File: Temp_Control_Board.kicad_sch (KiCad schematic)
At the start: 34 parts, among them J1 OVEN_INTERFACE, J2 OLED, J3 USB_B_Micro, J4 MICROSD, SW1 BOOT, SW2 EN, U1 ESP-WROOM-32, U2 AZ1117EH-3.3TRG1, U3 ROTARY_ENC_PEC12R, U4 FT232RLREEL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

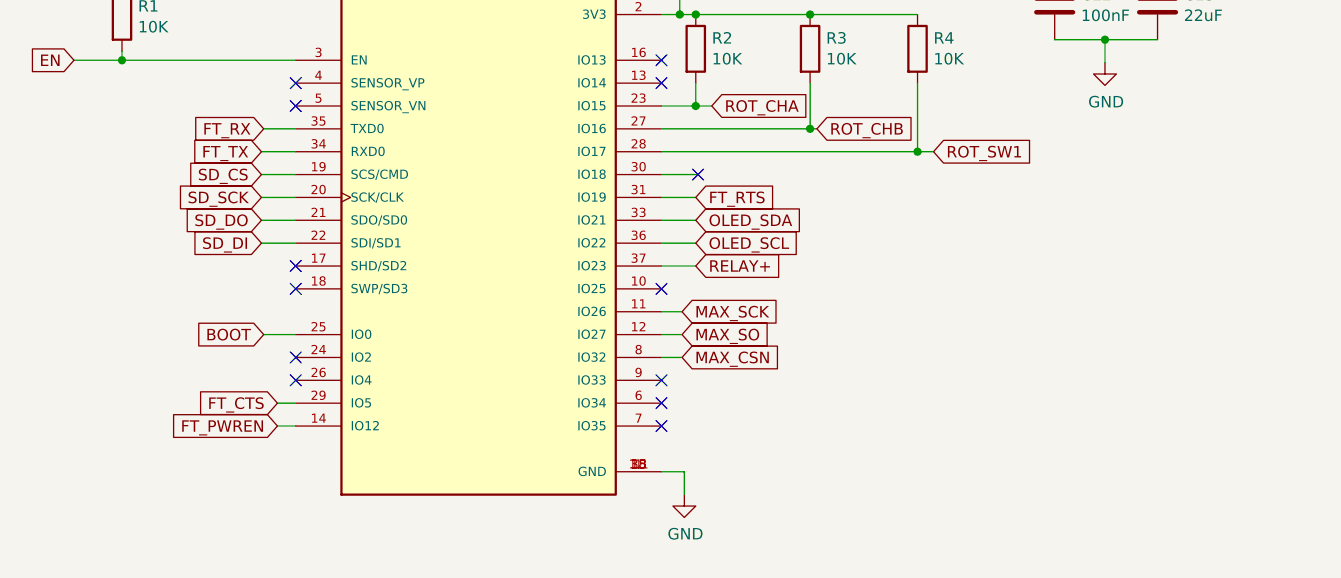
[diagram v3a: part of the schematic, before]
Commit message: sch: changed SD card pis to use SPI3 (VSPI)
    - Moved FT232 RTS and CTS pins to floating for now. These
      should be tied into the reset-esp32-via-UART circuit
      anyway
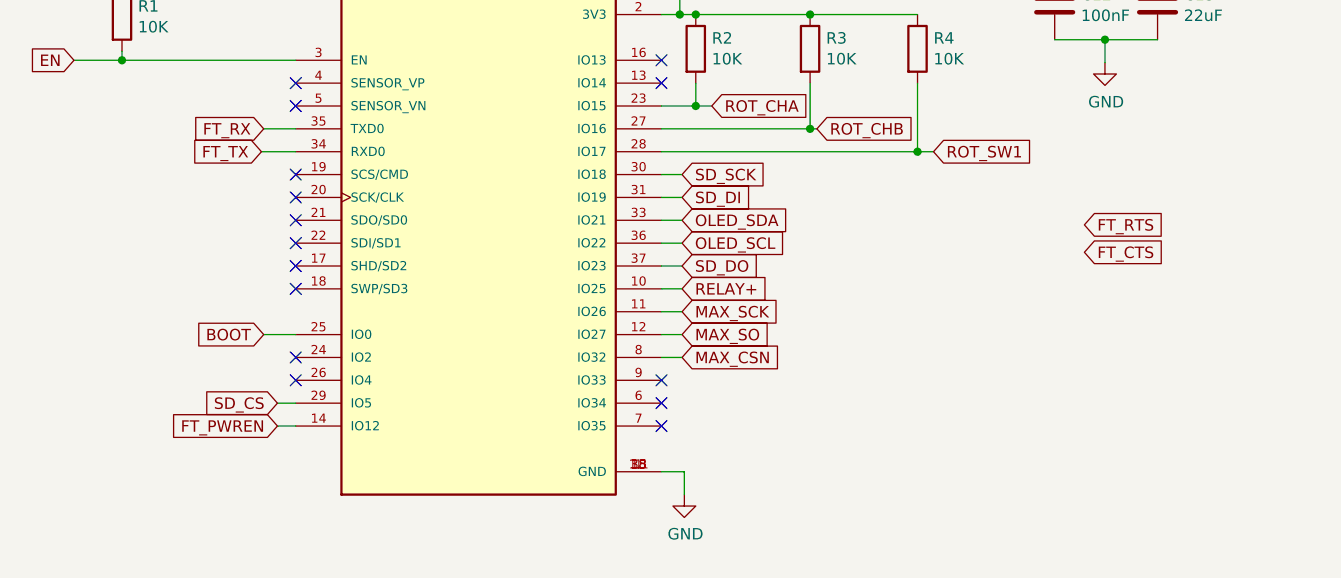
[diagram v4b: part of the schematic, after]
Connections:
- net FT_CTS: no longer U1.29 (IO5)
- net FT_RTS: no longer U1.31 (IO19)
- net RELAY+: now also U1.10 (IO25); no longer U1.37 (IO23)
- net SD_CS: now also U1.29 (IO5); no longer U1.19 (SCS/CMD)
- net SD_DI: now also U1.31 (IO19); no longer U1.22 (SDI/SD1)
- net SD_DO: now also U1.37 (IO23); no longer U1.21 (SDO/SD0)
- net SD_SCK: now also U1.30 (IO18); no longer U1.20 (SCK/CLK)
- no-connect marks 26 -> 28
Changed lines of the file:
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@@
   (junction (at 153.416 44.196) (diameter 0) (color 0 0 0 0)
   )
+  (no_connect (at 63.5 61.722))
+  (no_connect (at 63.5 66.802))
+  (no_connect (at 104.14 87.122))
   (no_connect (at 330.708 53.086))
+  (no_connect (at 63.5 64.262))
   (no_connect (at 284.988 60.706))
   (no_connect (at 104.14 46.482))
@@
   (no_connect (at 104.14 82.042))
   (no_connect (at 73.406 224.536))
+  (no_connect (at 63.5 69.342))
+  (no_connect (at 63.5 71.882))
   (no_connect (at 63.5 82.042))
   (no_connect (at 63.5 51.562))
-  (no_connect (at 104.14 87.122))
   (no_connect (at 104.14 49.022))
   (no_connect (at 330.708 48.006))
   (no_connect (at 284.988 73.406))
-  (no_connect (at 63.5 71.882))
   (no_connect (at 284.988 63.246))
   (no_connect (at 330.708 73.406))
-  (no_connect (at 63.5 69.342))
   (no_connect (at 284.988 53.086))
+  (no_connect (at 63.5 59.182))
   (no_connect (at 104.14 84.582))
-  (no_connect (at 108.204 59.182))
   (no_connect (at 63.5 49.022))
   (no_connect (at 330.708 63.246))
-  (no_connect (at 104.14 71.882))
   (no_connect (at 63.5 79.502))
   (polyline (pts (xy 223.774 117.094) (xy 302.26 117.094))
@@
     (stroke (width 0) (type default) (color 0 0 0 0))
   )
-  (wire (pts (xy 59.69 61.722) (xy 63.5 61.722))
-    (stroke (width 0) (type default) (color 0 0 0 0))
-  )
   (wire (pts (xy 251.714 82.55) (xy 245.618 82.55))
     (stroke (width 0) (type default) (color 0 0 0 0))
@@
     (stroke (width 0) (type default) (color 0 0 0 0))
   )
-  (wire (pts (xy 104.14 69.342) (xy 107.95 69.342))
-    (stroke (width 0) (type default) (color 0 0 0 0))
-  )
   (wire (pts (xy 153.416 44.196) (xy 153.416 46.736))
     (stroke (width 0) (type default) (color 0 0 0 0))
@@
     (stroke (width 0) (type default) (color 0 0 0 0))
   )
+  (wire (pts (xy 104.14 66.802) (xy 106.426 66.802))
+    (stroke (width 0) (type default) (color 0 0 0 0))
+  )
   (polyline (pts (xy 162.56 142.748) (xy 208.28 142.748))
     (stroke (width 0) (type default) (color 0 0 0 0))
@@
     (stroke (width 0) (type default) (color 0 0 0 0))
   )
+  (wire (pts (xy 104.14 61.722) (xy 106.426 61.722))
+    (stroke (width 0) (type default) (color 0 0 0 0))
+  )
   (polyline (pts (xy 302.26 117.094) (xy 302.26 153.924))
     (stroke (width 0) (type default) (color 0 0 0 0))
@@
     (stroke (width 0) (type default) (color 0 0 0 0))
   )
-  (wire (pts (xy 59.69 64.262) (xy 63.5 64.262))
-    (stroke (width 0) (type default) (color 0 0 0 0))
-  )
   (wire (pts (xy 147.828 44.196) (xy 153.416 44.196))
     (stroke (width 0) (type default) (color 0 0 0 0))
@@
     (stroke (width 0) (type default) (color 0 0 0 0))
   )
+  (wire (pts (xy 104.14 71.882) (xy 106.426 71.882))
+    (stroke (width 0) (type default) (color 0 0 0 0))
+  )
   (wire (pts (xy 138.43 141.732) (xy 147.574 141.732))
     (stroke (width 0) (type default) (color 0 0 0 0))
@@
     (stroke (width 0) (type default) (color 0 0 0 0))
   )
-  (wire (pts (xy 59.69 59.182) (xy 63.5 59.182))
-    (stroke (width 0) (type default) (color 0 0 0 0))
-  )
-  (wire (pts (xy 59.69 66.802) (xy 63.5 66.802))
-    (stroke (width 0) (type default) (color 0 0 0 0))
-  )
   (wire (pts (xy 284.988 68.326) (xy 284.988 70.866))
     (stroke (width 0) (type default) (color 0 0 0 0))
@@
     (stroke (width 0) (type default) (color 0 0 0 0))
   )
-  (wire (pts (xy 108.204 59.182) (xy 104.14 59.182))
-    (stroke (width 0) (type default) (color 0 0 0 0))
-  )
   (polyline (pts (xy 208.28 123.19) (xy 162.56 123.19))
     (stroke (width 0) (type default) (color 0 0 0 0))
@@
     (stroke (width 0) (type default) (color 0 0 0 0))
   )
-  (wire (pts (xy 104.14 61.722) (xy 107.95 61.722))
-    (stroke (width 0) (type default) (color 0 0 0 0))
-  )
   (wire (pts (xy 70.358 151.638) (xy 70.358 154.178))
     (stroke (width 0) (type default) (color 0 0 0 0))
@@
     (stroke (width 0) (type default) (color 0 0 0 0))
   )
+  (wire (pts (xy 104.14 69.342) (xy 106.426 69.342))
+    (stroke (width 0) (type default) (color 0 0 0 0))
+  )
   (wire (pts (xy 284.988 50.546) (xy 280.162 50.546))
     (stroke (width 0) (type default) (color 0 0 0 0))
@@
     (stroke (width 0) (type default) (color 0 0 0 0))
   )
-  (wire (pts (xy 104.14 66.802) (xy 107.95 66.802))
-    (stroke (width 0) (type default) (color 0 0 0 0))
-  )
   (wire (pts (xy 272.288 48.006) (xy 284.988 48.006))
     (stroke (width 0) (type default) (color 0 0 0 0))
@@
     (stroke (width 0) (type default) (color 0 0 0 0))
   )
+  (wire (pts (xy 104.14 59.182) (xy 106.426 59.182))
+    (stroke (width 0) (type default) (color 0 0 0 0))
+  )
   (polyline (pts (xy 154.432 151.384) (xy 154.432 121.158))
     (stroke (width 0) (type default) (color 0 0 0 0))
@@
     (stroke (width 0) (type default) (color 0 0 0 0))
   )
-  (wire (pts (xy 107.95 64.262) (xy 104.14 64.262))
+  (wire (pts (xy 104.14 64.262) (xy 106.426 64.262))
     (stroke (width 0) (type default) (color 0 0 0 0))
   )
@@
     (effects (font (size 1.27 1.27)) (justify left bottom))
   )
-  (global_label "RELAY+" (shape input) (at 107.95 69.342 0) (fields_autoplaced)
-    (effects (font (size 1.27 1.27)) (justify left))
-    (property "Intersheet References" "${INTERSHEET_REFS}" (id 0) (at 0 0 0)
-      (effects (font (size 1.27 1.27)) hide)
-    )
-  )
-  (global_label "FT_CTS" (shape input) (at 61.468 84.582 180) (fields_autoplaced)
-    (effects (font (size 1.27 1.27)) (justify right))
-    (property "Intersheet References" "${INTERSHEET_REFS}" (id 0) (at 0 0 0)
+  (global_label "RELAY+" (shape input) (at 106.426 71.882 0) (fields_autoplaced)
+    (effects (font (size 1.27 1.27)) (justify left))
+    (property "Intersheet References" "${INTERSHEET_REFS}" (id 0) (at -1.524 2.54 0)
+      (effects (font (size 1.27 1.27)) hide)
+    )
+  )
+  (global_label "FT_CTS" (shape input) (at 151.13 67.818 0) (fields_autoplaced)
+    (effects (font (size 1.27 1.27)) (justify left))
+    (property "Intersheet References" "${INTERSHEET_REFS}" (id 0) (at 212.598 152.4 0)
       (effects (font (size 1.27 1.27)) hide)
     )
@@
     )
   )
-  (global_label "SD_CS" (shape input) (at 59.69 59.182 180) (fields_autoplaced)
-    (effects (font (size 1.27 1.27)) (justify right))
-    (property "Intersheet References" "${INTERSHEET_REFS}" (id 0) (at 0 0 0)
+  (global_label "SD_CS" (shape input) (at 61.468 84.582 180) (fields_autoplaced)
+    (effects (font (size 1.27 1.27)) (justify right))
+    (property "Intersheet References" "${INTERSHEET_REFS}" (id 0) (at 1.778 25.4 0)
       (effects (font (size 1.27 1.27)) hide)
     )
@@
     )
   )
-  (global_label "SD_SCK" (shape input) (at 59.69 61.722 180) (fields_autoplaced)
-    (effects (font (size 1.27 1.27)) (justify right))
-    (property "Intersheet References" "${INTERSHEET_REFS}" (id 0) (at 0 0 0)
-      (effects (font (size 1.27 1.27)) hide)
-    )
-  )
-  (global_label "OLED_SCL" (shape input) (at 107.95 66.802 0) (fields_autoplaced)
-    (effects (font (size 1.27 1.27)) (justify left))
-    (property "Intersheet References" "${INTERSHEET_REFS}" (id 0) (at 0 0 0)
+  (global_label "SD_SCK" (shape input) (at 106.426 59.182 0) (fields_autoplaced)
+    (effects (font (size 1.27 1.27)) (justify left))
+    (property "Intersheet References" "${INTERSHEET_REFS}" (id 0) (at 166.116 120.904 0)
+      (effects (font (size 1.27 1.27)) hide)
+    )
+  )
+  (global_label "OLED_SCL" (shape input) (at 106.426 66.802 0) (fields_autoplaced)
+    (effects (font (size 1.27 1.27)) (justify left))
+    (property "Intersheet References" "${INTERSHEET_REFS}" (id 0) (at -1.524 0 0)
       (effects (font (size 1.27 1.27)) hide)
     )
@@
     )
   )
-  (global_label "OLED_SDA" (shape input) (at 107.95 64.262 0) (fields_autoplaced)
-    (effects (font (size 1.27 1.27)) (justify left))
-    (property "Intersheet References" "${INTERSHEET_REFS}" (id 0) (at 0 0 0)
+  (global_label "OLED_SDA" (shape input) (at 106.426 64.262 0) (fields_autoplaced)
+    (effects (font (size 1.27 1.27)) (justify left))
+    (property "Intersheet References" "${INTERSHEET_REFS}" (id 0) (at -1.524 0 0)
       (effects (font (size 1.27 1.27)) hide)
     )
@@
     )
   )
-  (global_label "FT_RTS" (shape input) (at 107.95 61.722 0) (fields_autoplaced)
-    (effects (font (size 1.27 1.27)) (justify left))
-    (property "Intersheet References" "${INTERSHEET_REFS}" (id 0) (at 0 0 0)
+  (global_label "FT_RTS" (shape input) (at 151.13 64.77 0) (fields_autoplaced)
+    (effects (font (size 1.27 1.27)) (justify left))
+    (property "Intersheet References" "${INTERSHEET_REFS}" (id 0) (at 43.18 3.048 0)
       (effects (font (size 1.27 1.27)) hide)
     )
@@
     )
   )
-  (global_label "SD_DO" (shape input) (at 59.69 64.262 180) (fields_autoplaced)
-    (effects (font (size 1.27 1.27)) (justify right))
-    (property "Intersheet References" "${INTERSHEET_REFS}" (id 0) (at 0 0 0)
+  (global_label "SD_DO" (shape input) (at 106.426 69.342 0) (fields_autoplaced)
+    (effects (font (size 1.27 1.27)) (justify left))
+    (property "Intersheet References" "${INTERSHEET_REFS}" (id 0) (at 166.116 133.604 0)
       (effects (font (size 1.27 1.27)) hide)
     )
@@
     )
   )
-  (global_label "SD_DI" (shape input) (at 59.69 66.802 180) (fields_autoplaced)
-    (effects (font (size 1.27 1.27)) (justify right))
-    (property "Intersheet References" "${INTERSHEET_REFS}" (id 0) (at 0 0 0)
-      (effects (font (size 1.27 1.27)) hide)
-    )
+  (global_label "SD_DI" (shape input) (at 106.426 61.722 0) (fields_autoplaced)
+    (effects (font (size 1.27 1.27)) (justify left))
+    (property "Intersheet References" "${INTERSHEET_REFS}" (id 0) (at 166.116 128.524 0)
+      (effects (font (size 1.27 1.27)) hide)
+    )

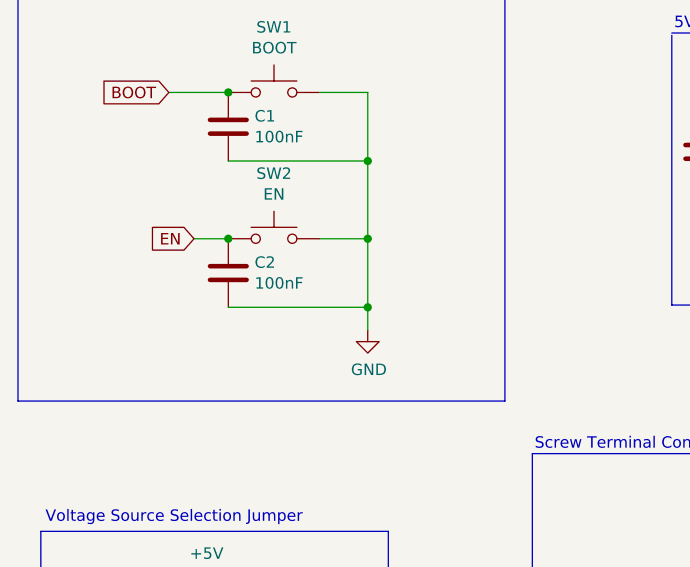
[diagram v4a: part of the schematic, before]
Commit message: sch: increased C between EN and GND
    - Necessary to increase capacitance for reset to work correctly
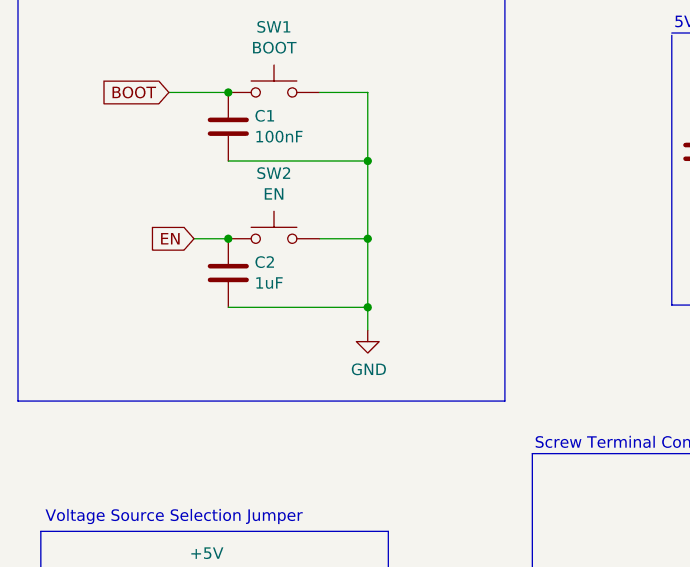
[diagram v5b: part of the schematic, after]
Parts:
- C2: value 100nF -> 1uF
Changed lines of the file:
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@@
       (effects (font (size 1.27 1.27)) (justify left))
     )
-    (property "Value" "100nF" (id 1) (at 57.785 148.971 0)
+    (property "Value" "1uF" (id 1) (at 57.785 148.971 0)
       (effects (font (size 1.27 1.27)) (justify left))
     )
@@
     )
     (path "/00000000-0000-0000-0000-0000607d89f7"
-      (reference "C2") (unit 1) (value "100nF") (footprint "Capacitor_SMD:C_0805_2012Metric_Pad1.15x1.40mm_HandSolder")
+      (reference "C2") (unit 1) (value "1uF") (footprint "Capacitor_SMD:C_0805_2012Metric_Pad1.15x1.40mm_HandSolder")
     )
     (path "/00000000-0000-0000-0000-0000607cc4d0"

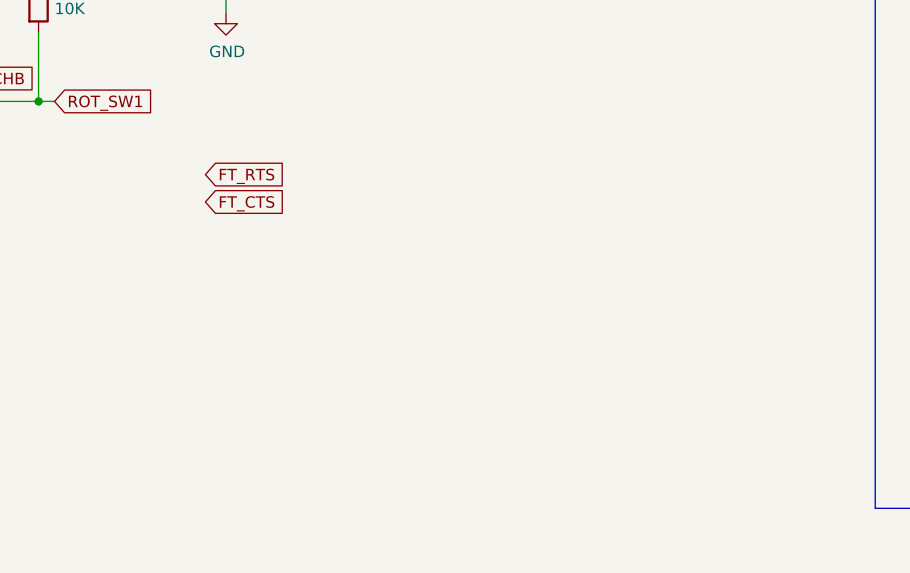
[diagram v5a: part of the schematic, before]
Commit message: Began adding reset circuit to schematic
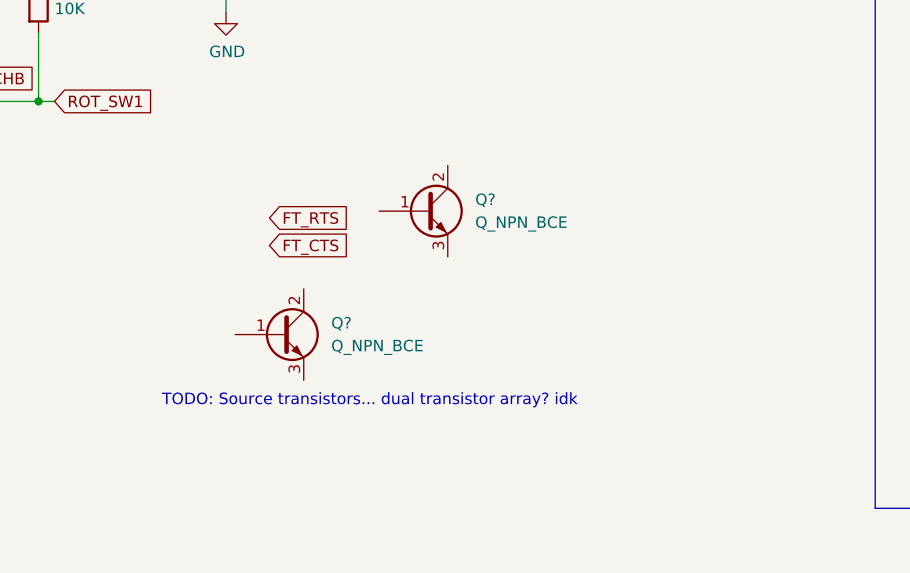
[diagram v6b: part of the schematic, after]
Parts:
- added Q? (x2): Q_NPN_BCE, symbol Device:Q_NPN_BCE
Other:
- note added: "TODO: Source transistors... dual transistor array? idk"
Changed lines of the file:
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@@
     (stroke (width 0) (type default) (color 0 0 0 0))
+  )
+  (text "TODO: Source transistors... dual transistor array? idk\n"
+    (at 146.304 90.678 0)
+    (effects (font (size 1.27 1.27)) (justify left bottom))
   )
   (text "Screw Terminal Connector" (at 88.9 167.64 0)
@@
     )
   )
-  (global_label "FT_CTS" (shape input) (at 151.13 67.818 0) (fields_autoplaced)
-    (effects (font (size 1.27 1.27)) (justify left))
-    (property "Intersheet References" "${INTERSHEET_REFS}" (id 0) (at 212.598 152.4 0)
+  (global_label "FT_CTS" (shape input) (at 158.242 72.644 0) (fields_autoplaced)
+    (effects (font (size 1.27 1.27)) (justify left))
+    (property "Intersheet References" "${INTERSHEET_REFS}" (id 0) (at 219.71 157.226 0)
       (effects (font (size 1.27 1.27)) hide)
     )
@@
     )
   )
-  (global_label "FT_RTS" (shape input) (at 151.13 64.77 0) (fields_autoplaced)
-    (effects (font (size 1.27 1.27)) (justify left))
-    (property "Intersheet References" "${INTERSHEET_REFS}" (id 0) (at 43.18 3.048 0)
+  (global_label "FT_RTS" (shape input) (at 158.242 69.596 0) (fields_autoplaced)
+    (effects (font (size 1.27 1.27)) (justify left))
+    (property "Intersheet References" "${INTERSHEET_REFS}" (id 0) (at 50.292 7.874 0)
       (effects (font (size 1.27 1.27)) hide)
     )
@@
     (pin "1")
   )
+  (symbol (lib_id "Device:Q_NPN_BCE") (at 159.512 82.55 0) (unit 1)
+    (in_bom yes) (on_board yes) (fields_autoplaced)
+    (property "Reference" "Q?" (id 0) (at 165.1 81.2799 0)
+      (effects (font (size 1.27 1.27)) (justify left))
+    )
+    (property "Value" "Q_NPN_BCE" (id 1) (at 165.1 83.8199 0)
+      (effects (font (size 1.27 1.27)) (justify left))
+    )
+    (property "Footprint" "" (id 2) (at 164.592 80.01 0)
+      (effects (font (size 1.27 1.27)) hide)
+    )
+    (property "Datasheet" "~" (id 3) (at 159.512 82.55 0)
+      (effects (font (size 1.27 1.27)) hide)
+    )
+    (pin "1")
+    (pin "2")
+    (pin "3")
+  )
+  (symbol (lib_id "Device:Q_NPN_BCE") (at 175.514 68.834 0) (unit 1)
+    (in_bom yes) (on_board yes) (fields_autoplaced)
+    (property "Reference" "Q?" (id 0) (at 181.102 67.5639 0)
+      (effects (font (size 1.27 1.27)) (justify left))
+    )
+    (property "Value" "Q_NPN_BCE" (id 1) (at 181.102 70.1039 0)
+      (effects (font (size 1.27 1.27)) (justify left))
+    )
+    (property "Footprint" "" (id 2) (at 180.594 66.294 0)
+      (effects (font (size 1.27 1.27)) hide)
+    )
+    (property "Datasheet" "~" (id 3) (at 175.514 68.834 0)
+      (effects (font (size 1.27 1.27)) hide)
+    )
+    (pin "1")
+    (pin "2")
+    (pin "3")
+  )
   (sheet_instances
     (path "/" (page "1"))
@@
       (reference "JP1") (unit 1) (value "JUMPER_5V_SEL") (footprint "Jumper:SolderJumper-3_P1.3mm_Open_Pad1.0x1.5mm")
     )
+    (path "/3dcdc3b1-d45a-4d49-ad2a-e6c281627928"
+      (reference "Q?") (unit 1) (value "Q_NPN_BCE") (footprint "")
+    )
+    (path "/b2e7a284-6d85-4550-826c-0ddf3595ce58"
+      (reference "Q?") (unit 1) (value "Q_NPN_BCE") (footprint "")
+    )
     (path "/00000000-0000-0000-0000-00006089f75d"
